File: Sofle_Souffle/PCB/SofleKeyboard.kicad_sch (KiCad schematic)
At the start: 97 parts, among them J2 4PIN, J3 OLED, J4 Conn_01x05_Female, P1 i2c_pin, P2 i2c_pin, P3 i2c_pin, P4 i2c_pin, P5 i2c_pin, P6 i2c_pin, P7 i2c_pin, P8 sw_pin, P9 sw_pin, SW1 SW_PUSH-MX_W_LED, SW10 SW_PUSH-MX_W_LED, SW11 SW_PUSH-MX_W_LED, SW12 SW_PUSH-MX_W_LED, SW13 SW_PUSH-MX_W_LED, SW14 SW_PUSH-MX_W_LED, SW15 SW_PUSH-MX_W_LED, SW16 SW_PUSH-MX_W_LED, SW17 SW_PUSH-MX_W_LED, SW18 SW_PUSH-MX_W_LED, SW19 SW_PUSH-MX_W_LED, SW2 SW_PUSH-MX_W_LED, SW20 SW_PUSH-MX_W_LED, SW21 SW_PUSH-MX_W_LED, SW22 SW_PUSH-MX_W_LED, SW23 SW_PUSH-MX_W_LED, SW24 SW_PUSH-MX_W_LED, SW25 Rotary_Encoder_Switch, SW25A1 SW_PUSH-MX_W_LED, SW26 SW_PUSH-MX_W_LED, SW27 SW_PUSH-MX_W_LED, SW28 SW_PUSH-MX_W_LED, SW29 SW_PUSH-MX_W_LED, SW3 SW_PUSH-MX_W_LED, SW30 SW_PUSH-MX_W_LED, SW4 SW_PUSH-MX_W_LED, SW5 SW_PUSH-MX_W_LED, SW6 SW_PUSH-MX_W_LED, SW7 SW_PUSH-MX_W_LED, SW8 SW_PUSH-MX_W_LED, SW9 SW_PUSH-MX_W_LED, U1 ProMicro

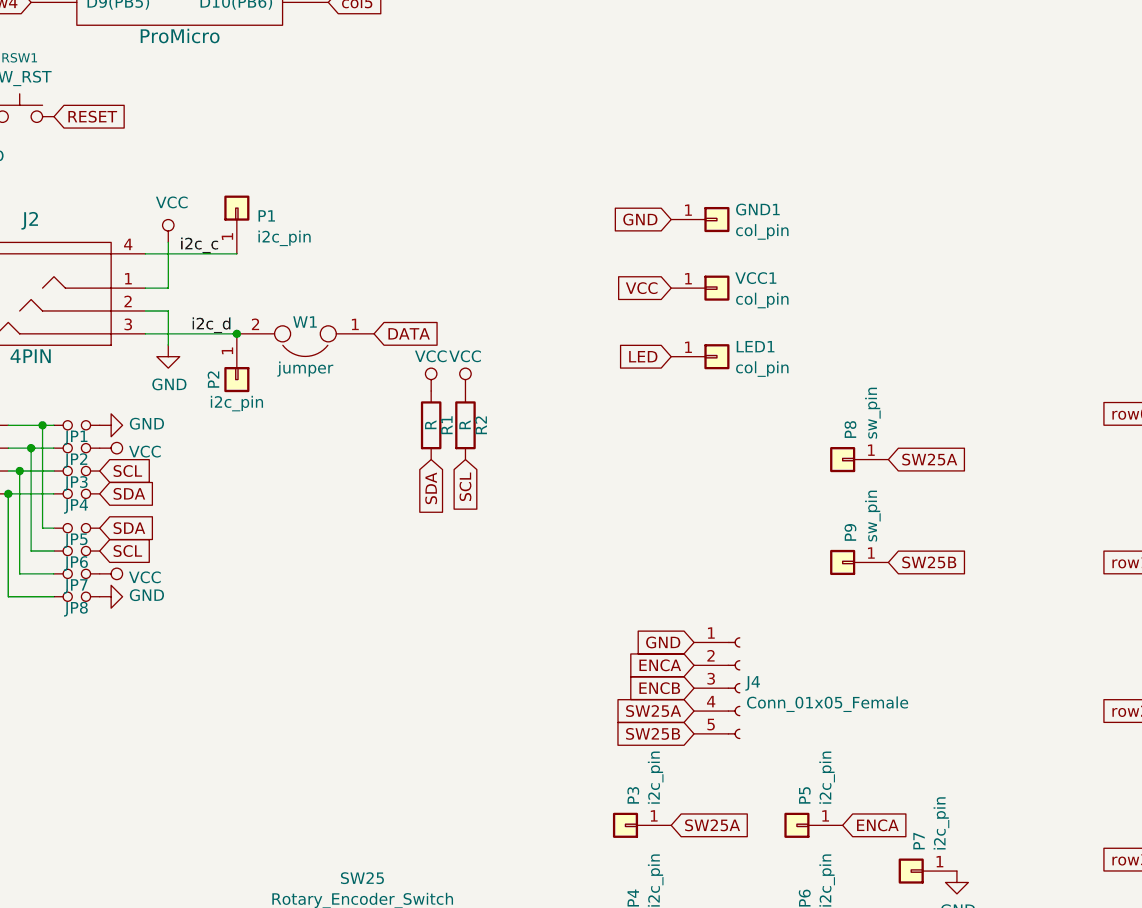
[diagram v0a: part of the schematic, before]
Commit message: Completed redesign of the roller encoder pins.
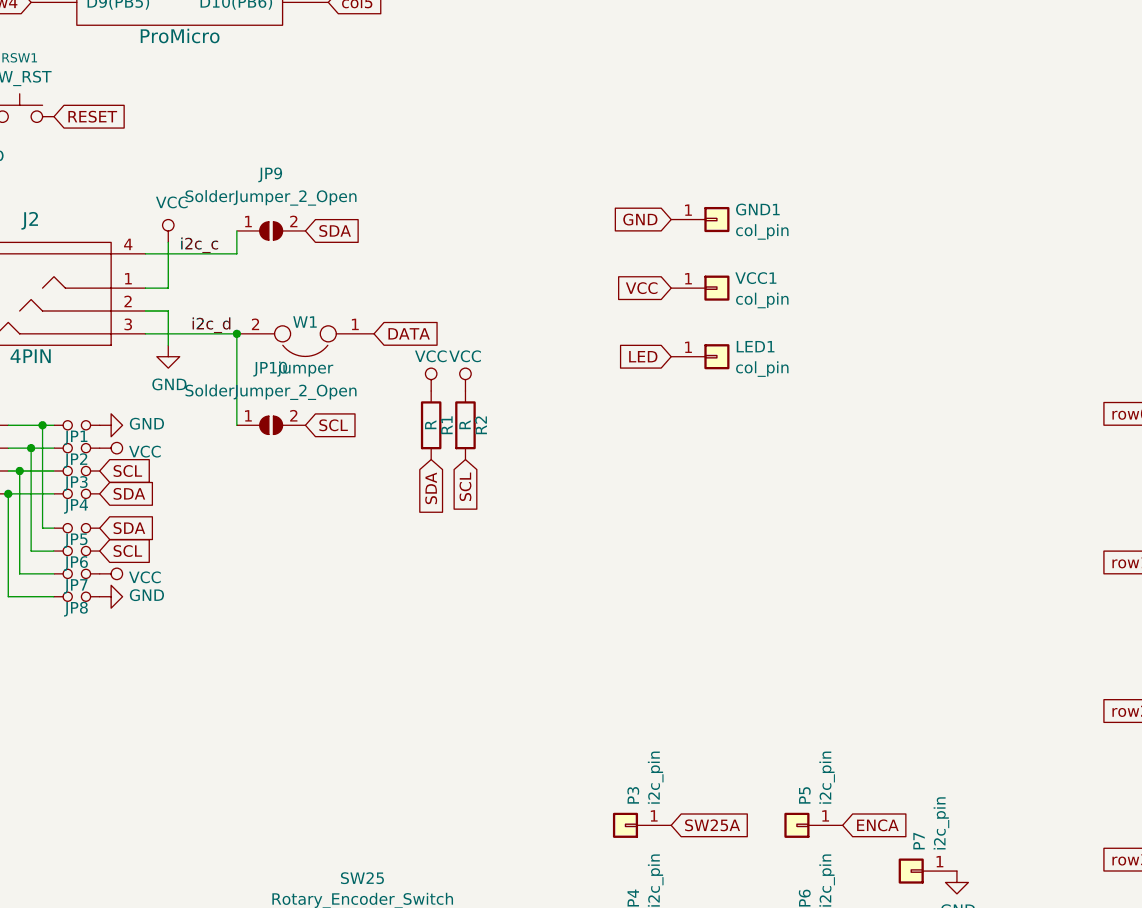
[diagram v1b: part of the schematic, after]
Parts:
- removed J4: Conn_01x05_Female, Connector_PinHeader_2.54mm:PinHeader_1x05_P2.54mm_Horizontal, symbol Connector:Conn_01x05_Female
- removed P1, P2: i2c_pin, SofleRGB:1pin_conn, symbol SofleKeyboard-rescue:i2c_pin-Lily58-cache-Lily58_Pro-rescue
- removed P8, P9: sw_pin, SofleRGB:Single_Hole, symbol SofleKeyboard-rescue:i2c_pin-Lily58-cache-Lily58_Pro-rescue
- added JP10, JP9: SolderJumper_2_Open, SofleRGB:Jumper, symbol Jumper:SolderJumper_2_Open
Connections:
- net SCL: now also JP10.2 (B)
- net SDA: now also JP9.2 (B)
- net i2c_c: now also JP9.1 (A)
- net i2c_d: now also JP10.1 (A)
